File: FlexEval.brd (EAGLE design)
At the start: 94.2 x 100 mm, 173 parts, among them J1 USB4105-GF-A, J2 GRPB052VWQS-RC, SW1 1825910-7, U1 MK22FX512AVLQ12, U3 IS31FL3733B-TQLS4, U4 IS31FL3733B-TQLS4, U5 SOIC127P600X175-8N, U6 AP2115M-3.3TRG1, Y1 ABM3B-8.000MHZ-B2-T, Y2 ABS07-32.768KHZ-T

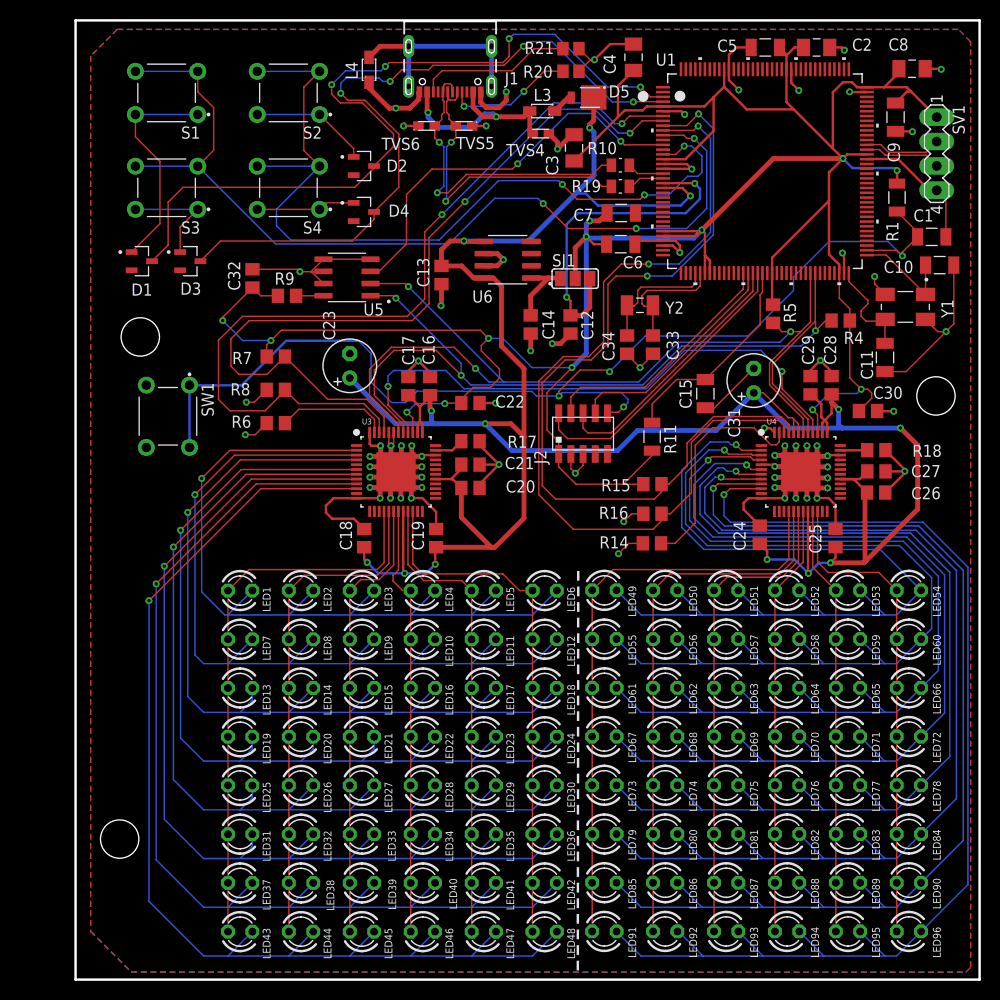
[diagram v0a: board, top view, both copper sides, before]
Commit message: schematic: update resistors and capacitors to Eagle libraries
Updated all resistors and capacitors to use Eagle libraries instead
of custom SnapEDA variants for each component. This should improve
flexibility of the design, since SMD packages for passives are standard
sizes.

Signed-off-by: Daniel DeGrasse <daniel@degrasse.com>
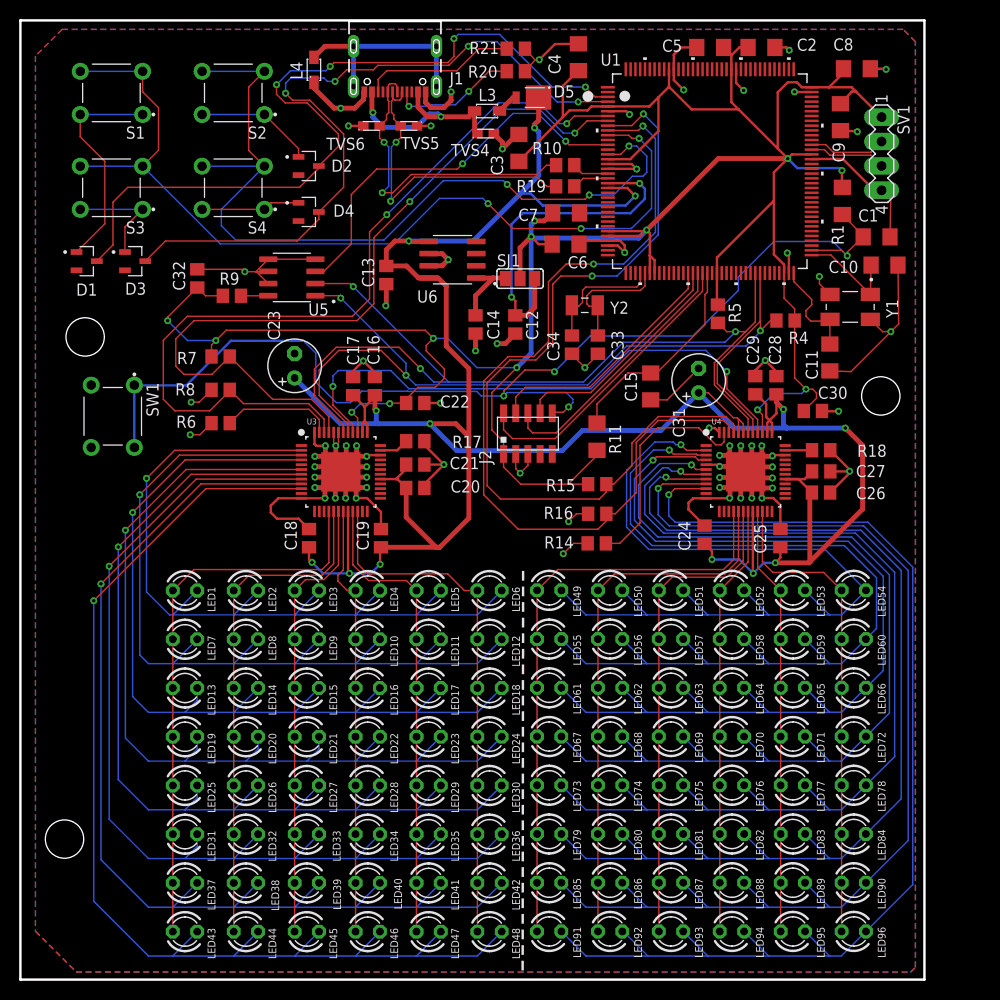
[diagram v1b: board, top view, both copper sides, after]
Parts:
- C1, C15: device C1206C102K1RACAUTO:CAPC3216X110N -> resistor:C1206
- C10, C11: device C1206C220JGGAC7800:CAPC3216X110N -> resistor:C1206
- C2, C3, C4, C8: device GCM31MR71H105KA55L:CAPC3216X125N -> resistor:C1206
- C5, C6, C7, C9: device C1206C104K5RAC7800:CAPC3216X88N -> resistor:C1206
- R1, R11: device CRGCQ1206J10K:RESC3115X65N -> resistor:R1206
- R10, R19: device CRG0805F33R:RESC2012X65N -> resistor:R0805
- R20, R21: device RNCP0805FTD20R0:RESC2012X60N -> resistor:R0805
- moved LED50 5.75 mm to (61.5, 40.6)
- moved LED56 5.75 mm to (61.5, 35.5)
- moved LED62 5.75 mm to (61.5, 30.4)
- moved LED68 5.75 mm to (61.5, 25.3)
- moved LED74 5.75 mm to (61.5, 20.3)
- moved LED80 5.75 mm to (61.5, 15.2)
- moved LED86 5.75 mm to (61.5, 10.1)
- moved LED92 5.75 mm to (61.5, 5.02)
- moved C18 5.75 mm to (30.1, 46.0)
- moved C23 5.75 mm to (28.6, 64.0)
- moved D2 5.75 mm to (30.1, 84.8)
- moved D4 5.75 mm to (30.1, 80.0)
- moved C1 5.75 mm to (89.3, 77.4)
- moved C10 5.75 mm to (90.1, 74.5)
- moved C11 5.75 mm to (84.4, 64.9)
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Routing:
- net VDD_3V3: track 310.8 -> 311.4 mm

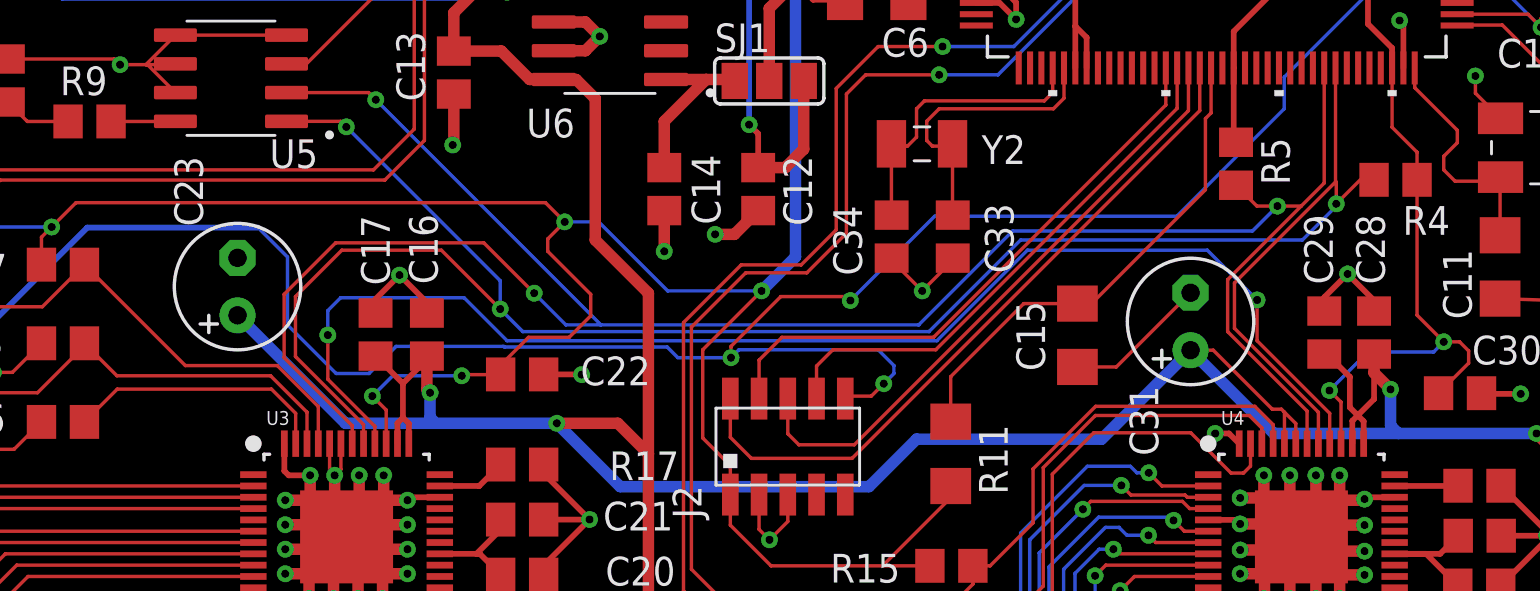
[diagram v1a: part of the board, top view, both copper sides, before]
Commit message: board: replaced Electrolytic Capactitors
Replaced electrolytic capacitors with real models, instead of
Eagle's default library

Signed-off-by: Daniel DeGrasse <daniel@degrasse.com>
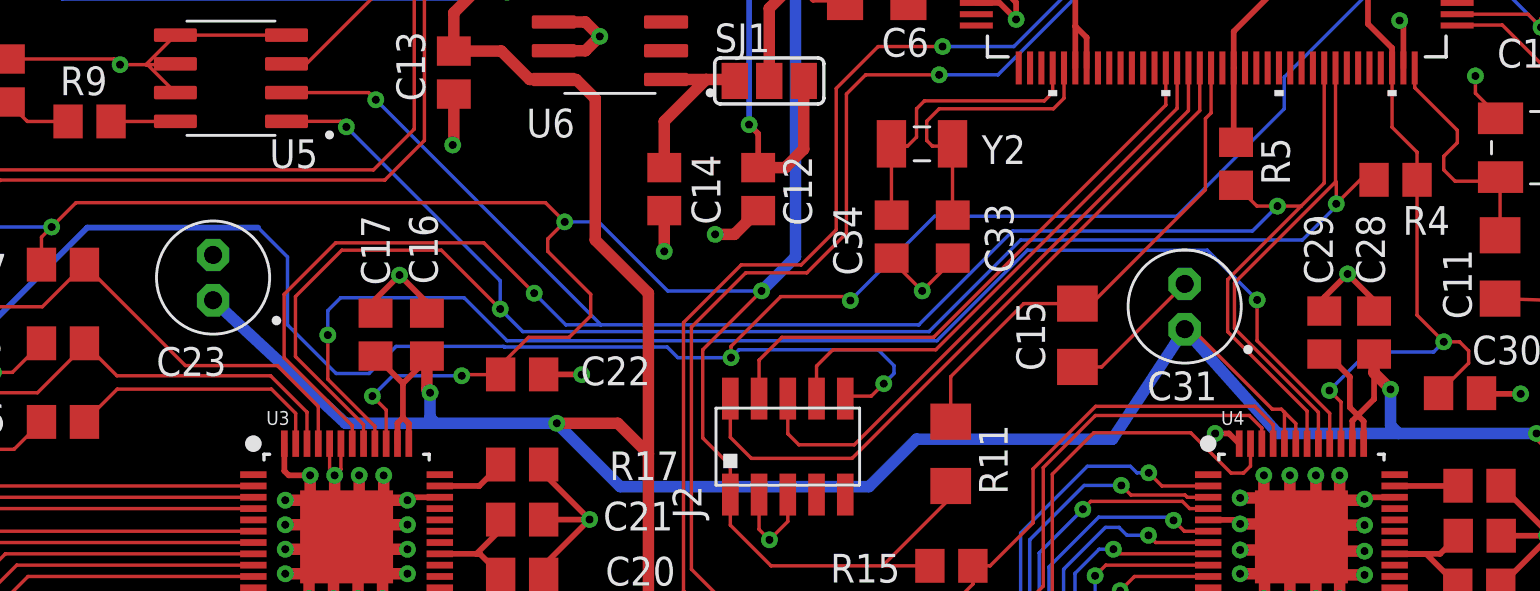
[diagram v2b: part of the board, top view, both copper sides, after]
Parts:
- C23, C31: device resistor:E2,5-6 -> 860020672011:860020672011
- moved C23 1.15 mm to (27.5, 64.4), turned to 180 degrees
- moved C31 0.71 mm to (70.5, 63.1), turned to 180 degrees
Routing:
- net VSYS_5V: track 273.7 -> 277.1 mm
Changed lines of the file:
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@@
 <attribute name="NAME" x="75.1" y="68.485" size="1.27" layer="25" rot="R90"/>
 </element>
-<element name="C23" library="resistor" library_urn="urn:adsk.eagle:library:348" package="E2,5-6" package3d_urn="urn:adsk.eagle:package:23349/1" value="22uF" x="28.59" y="63.99" smashed="yes" rot="R90">
-<attribute name="NAME" x="27.066" y="66.657" size="1.27" layer="25" ratio="10" rot="R90"/>
+<element name="C23" library="860020672011" package="860020672011" value="22uF" x="27.51" y="64.39" smashed="yes" rot="R180">
+<attribute name="NAME" x="28.093" y="61.316" size="1.27" layer="25" ratio="10" rot="R180"/>
 </element>
 <element name="R6" library="resistor" library_urn="urn:adsk.eagle:library:348" package="R0805" package3d_urn="urn:adsk.eagle:package:23553/2" value="100K" x="20.875" y="58.01" smashed="yes">
@@
 <attribute name="NAME" x="83.15" y="60.55" size="1.27" layer="25"/>
 </element>
-<element name="C31" library="resistor" library_urn="urn:adsk.eagle:library:348" package="E2,5-6" package3d_urn="urn:adsk.eagle:package:23349/1" value="22uF" x="70.71" y="62.45" smashed="yes" rot="R90">
-<attribute name="NAME" x="69.286" y="56.517" size="1.27" layer="25" ratio="10" rot="R90"/>
+<element name="C31" library="860020672011" package="860020672011" value="22uF" x="70.45" y="63.11" smashed="yes" rot="R180">
+<attribute name="NAME" x="71.883" y="60.236" size="1.27" layer="25" ratio="10" rot="R180"/>
 </element>
 <element name="R14" library="resistor" library_urn="urn:adsk.eagle:library:348" package="R0805" package3d_urn="urn:adsk.eagle:package:23553/2" value="100K" x="60.09" y="45.48" smashed="yes">
@@
 <wire x1="44.15" y1="90.9" x2="42.8" y2="90.9" width="0.508" layer="1"/>
 <wire x1="42.8" y1="90.9" x2="42.239" y2="91.461" width="0.508" layer="1"/>
-<wire x1="65.71" y1="60.44" x2="67.43" y2="60.44" width="0.1524" layer="1"/>
-<wire x1="67.43" y1="60.44" x2="70.71" y2="63.72" width="0.1524" layer="1"/>
+<wire x1="65.71" y1="60.44" x2="66.78" y2="60.44" width="0.1524" layer="1"/>
+<wire x1="66.78" y1="60.44" x2="70.45" y2="64.11" width="0.1524" layer="1"/>
 </signal>
 <signal name="JTAG_TCLK/SWD_CLK">
@@
 <wire x1="42.7" y1="57.95" x2="37.35" y2="57.95" width="0.508" layer="16"/>
 <wire x1="37.35" y1="57.95" x2="33.36" y2="57.95" width="0.508" layer="16"/>
-<wire x1="33.36" y1="57.95" x2="28.59" y2="62.72" width="0.508" layer="16"/>
+<wire x1="33.36" y1="57.95" x2="27.51" y2="63.39" width="0.508" layer="16"/>
 <wire x1="37.35" y1="57.95" x2="37.1" y2="58.2" width="0.508" layer="16"/>
 <wire x1="37.1" y1="58.2" x2="37.1" y2="59.3" width="0.508" layer="16"/>
@@
 <wire x1="78.82" y1="59.02" x2="78.82" y2="60.6" width="0.254" layer="1"/>
 <wire x1="78.82" y1="60.6" x2="78.82" y2="61.01" width="0.254" layer="1"/>
-<wire x1="74.32256875" y1="58.57256875" x2="71.7151375" y2="61.18" width="0.1524" layer="1"/>
-<wire x1="71.7151375" y1="61.18" x2="70.71" y2="61.18" width="0.1524" layer="1"/>
 <wire x1="75.36" y1="57.05" x2="75.36" y2="57.94" width="0.1524" layer="1"/>
 <wire x1="74.72743125" y1="58.57256875" x2="74.32256875" y2="58.57256875" width="0.1524" layer="1"/>
@@
 <via x="86" y="57.5" extent="1-16" drill="0.35"/>
 <wire x1="86" y1="57.5" x2="79.9" y2="57.5" width="0.508" layer="16"/>
-<wire x1="79.9" y1="57.5" x2="74.39" y2="57.5" width="0.508" layer="16"/>
-<wire x1="74.39" y1="57.5" x2="70.71" y2="61.18" width="0.508" layer="16"/>
+<wire x1="79.9" y1="57.5" x2="74.561621875" y2="57.5" width="0.508" layer="16"/>
+<wire x1="74.561621875" y1="57.5" x2="70.45" y2="62.11" width="0.508" layer="16"/>
 <wire x1="79.9" y1="57.5" x2="79.55" y2="57.85" width="0.508" layer="16"/>
 <wire x1="79.55" y1="57.85" x2="79.55" y2="59.45" width="0.508" layer="16"/>
@@
 <wire x1="46.75" y1="56.6" x2="46.75" y2="48.1" width="0.508" layer="1"/>
 <wire x1="45.5" y1="55.15" x2="42.7" y2="57.95" width="0.508" layer="16"/>
-<wire x1="70.71" y1="61.18" x2="66.78" y2="57.25" width="0.508" layer="16"/>
-<wire x1="66.78" y1="57.25" x2="58.6" y2="57.25" width="0.508" layer="16"/>
+<wire x1="70.45" y1="62.11" x2="67.261225" y2="57.25" width="0.508" layer="16"/>
+<wire x1="67.261225" y1="57.25" x2="58.6" y2="57.25" width="0.508" layer="16"/>
 <wire x1="58.6" y1="57.25" x2="56.5" y2="55.15" width="0.508" layer="16"/>
 <wire x1="56.5" y1="55.15" x2="45.5" y2="55.15" width="0.508" layer="16"/>
@@
 <wire x1="77.75" y1="60" x2="76.76" y2="60.99" width="0.254" layer="1"/>
 <wire x1="76.76" y1="60.99" x2="76.6" y2="60.99" width="0.254" layer="1"/>
+<wire x1="70.7851375" y1="62.11" x2="70.45" y2="62.11" width="0.1524" layer="1"/>
+<wire x1="74.32256875" y1="58.57256875" x2="70.7851375" y2="62.11" width="0.1524" layer="1"/>
 </signal>
 <signal name="INTB_LED_CTRL_1">

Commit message: board: added test points and debug LEDs
Added two debug LEDs, and test points on I2C and voltage signals. BOM
updated with 2 additional 200 Ohm resistors and 2 1206 LEDs

Signed-off-by: Daniel DeGrasse <daniel@degrasse.com>
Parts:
- added LED97: GREEN, led:SML1206
- added LED98: RED, led:SML1206
- added R2, R3: 200, resistor:R0805
- added TP1, TP2, TP3, TP4, TP5: TPSQTP20R, testpad:TP20R
- moved R11 1.60 mm to (61.7, 56.6)
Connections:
- new net MCU_LED1: R2.2, U1.45
- new net MCU_LED2: R3.2, U1.46
- new net N$1: LED97.A, R2.1
- new net N$2: LED98.A, R3.1
- net GND: now also LED97.C, LED98.C
- net I2C2_SCL: now also TP5.TP
- net I2C2_SDA: now also TP4.TP
- net VBUS: now also TP2.TP
- net VDD_3V3: now also TP3.TP
- net VSYS_5V: now also TP1.TP
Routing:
- net MCU_LED2: track 0.00 -> 42.2 mm, vias 0 -> 4
- net MCU_LED1: track 0.00 -> 40.1 mm, vias 0 -> 4
- net N$1: track 0.00 -> 27.6 mm, vias 0 -> 2
- net N$2: track 0.00 -> 26.9 mm, vias 0 -> 2
- net GND: track 290.1 -> 299.1 mm, vias 68 -> 70
- net VDD_3V3: track 311.4 -> 315.5 mm
- net I2C2_SCL: track 97.6 -> 99.8 mm
- net VSYS_5V: track 277.1 -> 275.5 mm
- net NMI: track 22.2 -> 20.5 mm
- net VBUS: track 21.6 -> 22.6 mm
- net INTB_LED_CTRL_1: track 84.7 -> 83.9 mm
- net SDB_LED_CTRL_1: track 88.9 -> 88.1 mm
